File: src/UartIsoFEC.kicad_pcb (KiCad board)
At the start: 2 copper layers, 24 x 27.9 mm, 28 parts, among them P1 105444-0001, U2 ADUM5211

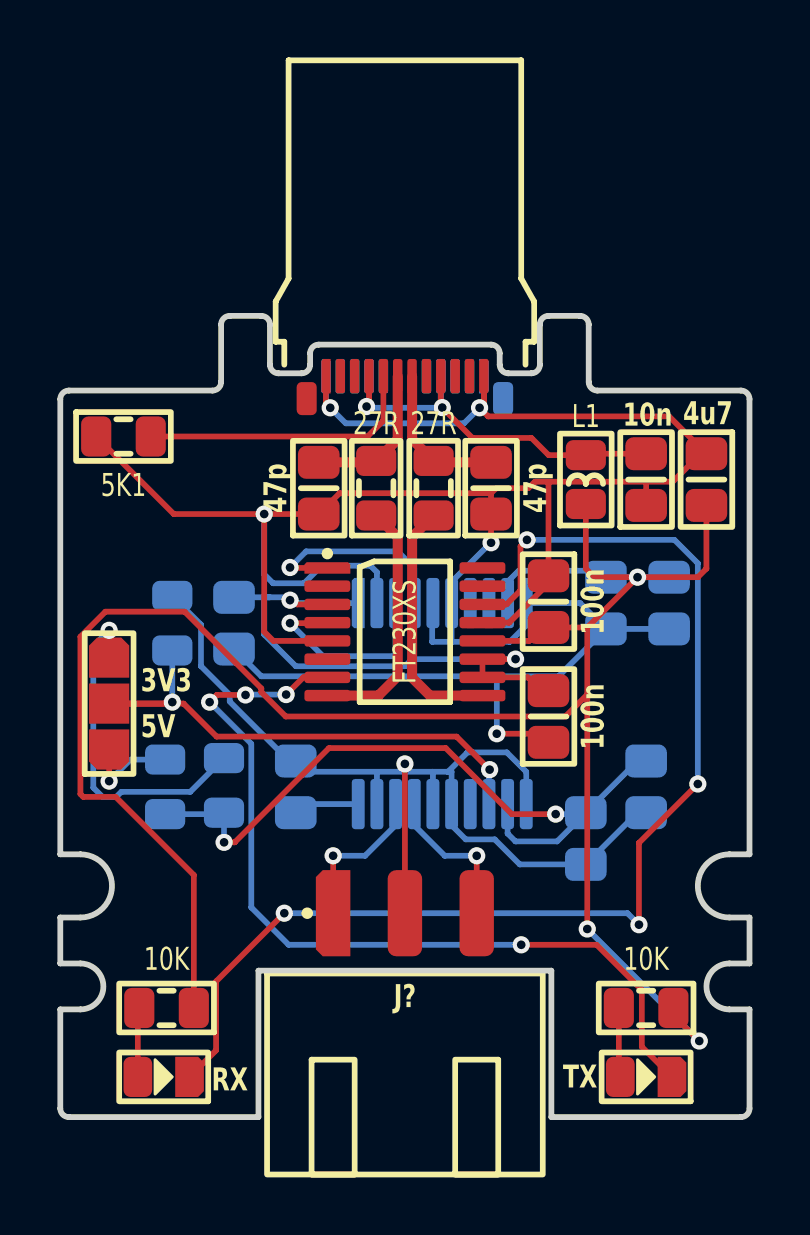
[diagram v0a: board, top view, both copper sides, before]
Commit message: New revision using FT260X
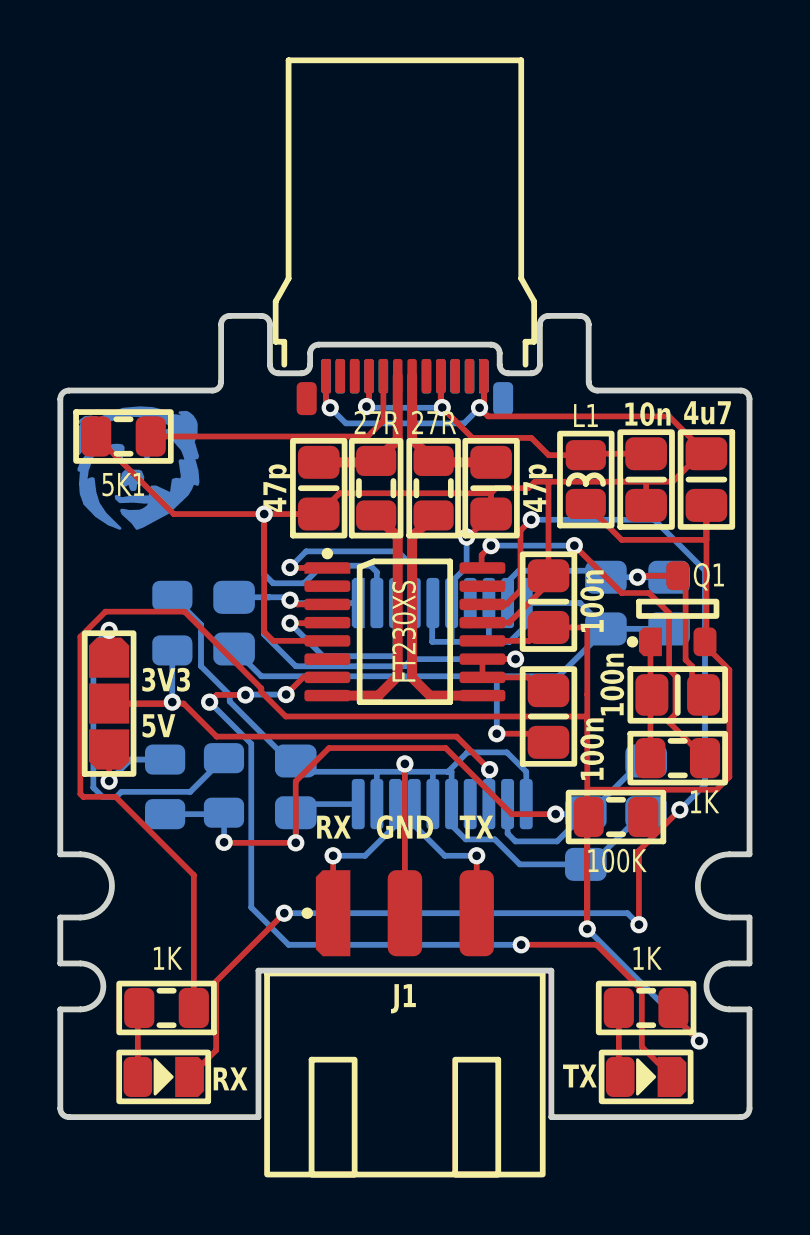
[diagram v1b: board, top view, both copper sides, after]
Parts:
- added C6: 100n, Medo64:C (0805), F.Cu at (41.5, 33.2)
- added ICON: Medo64, Medo64:ICON Medo64, B.Cu at (22.7, 25.3)
- added Q1: DMP3099L-13, Medo64:Q MOSFET-P (SOT23-3), F.Cu at (41.5, 30.2)
- added R10: 100K, Medo64:R (0805), F.Cu at (39.4, 37.5)
- added R5: 1K, Medo64:R (0805), F.Cu at (41.5, 35.4)
- L1: value 1u -> 600R
- R3, R4: renamed from R?; value 10K -> 1K
- gave numbers to parts that had none: 23
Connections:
- C10 pad 2: B_3V3 -> B_VISO
- C12 pad 2: A_5V -> A_5V_SWITCHED
- C7 pad 2: A_5V -> A_5V_SWITCHED
- U1 pad 16: (no net) -> PWREN_NEG
- U2 pad 20: B_3V3 -> B_VISO
- U2 pad 8: (no net) -> A_GND
- U2 pad 9: A_5V -> A_5V_SWITCHED
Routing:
- net PWREN_NEG: track 0.00 -> 13.8 mm, vias 0 -> 2
- net A_5V_SWITCHED: track 0.00 -> 10.5 mm, vias 0 -> 1
- net A_5V: track 73.5 -> 80.5 mm, vias 3 -> 2
- net PWREN_NEG': track 0.00 -> 4.00 mm
- net B_VISO: track 25.4 -> 28.4 mm, vias 2 -> 3
- net B_3V3: track 1.88 -> 0.00 mm
- net A_GND: track 96.5 -> 97.8 mm
- net A_LED_RX: track 42.7 -> 43.8 mm
- net B_GND: track 34.1 -> 33.5 mm
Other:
- board text added: "GND"
- board text added: "RX"
- board text added: "TX"
- board text added: "UartIsoFEC B"

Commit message: Added protection diode
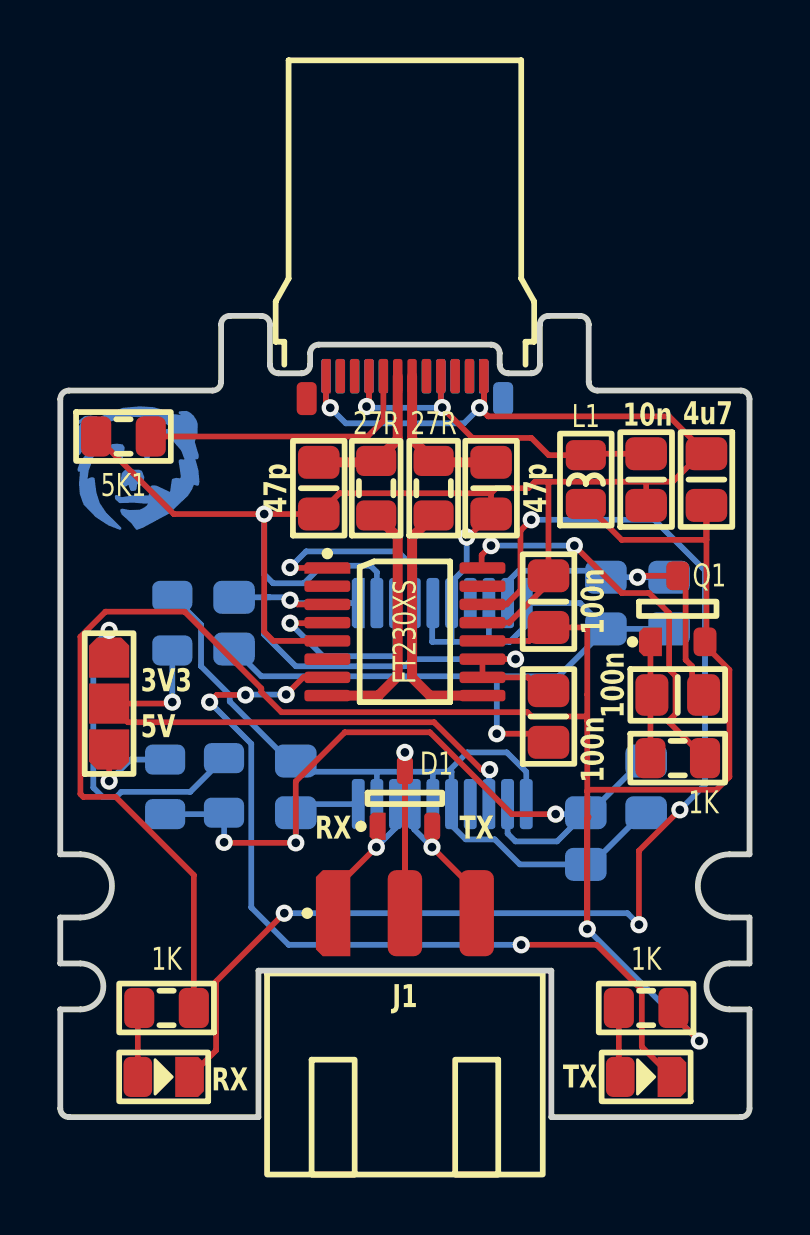
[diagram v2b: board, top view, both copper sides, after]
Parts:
- removed R10: 100K, Medo64:R (0805)
- added D1: SM05T1G, Medo64:D TVS SM05T1G (SOT23-3), F.Cu at (32.0, 36.8)
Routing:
- net B_GND: track 33.5 -> 39.5 mm
- net B_RX: track 4.62 -> 3.91 mm
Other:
- board text removed: "GND"
